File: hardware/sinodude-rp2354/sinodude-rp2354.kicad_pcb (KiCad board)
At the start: 2 copper layers, 68 x 36 mm, 93 parts, among them J1 USB-C, J2 SWD TC2030-IDC latching, J4 DUT, Q1 2N7002, SW1 BOOTSEL, SW2 RESET, U1 RP2354A, U2 AMS1117-3.3, U3 TPS2114APW, U4 SN74LVC8T245PW, U5 SN74LVC1T45DBV, U6 SN74LVC1T45DBV, Y1 12MHz/CL10pF/ESR50R/ABM8-272-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

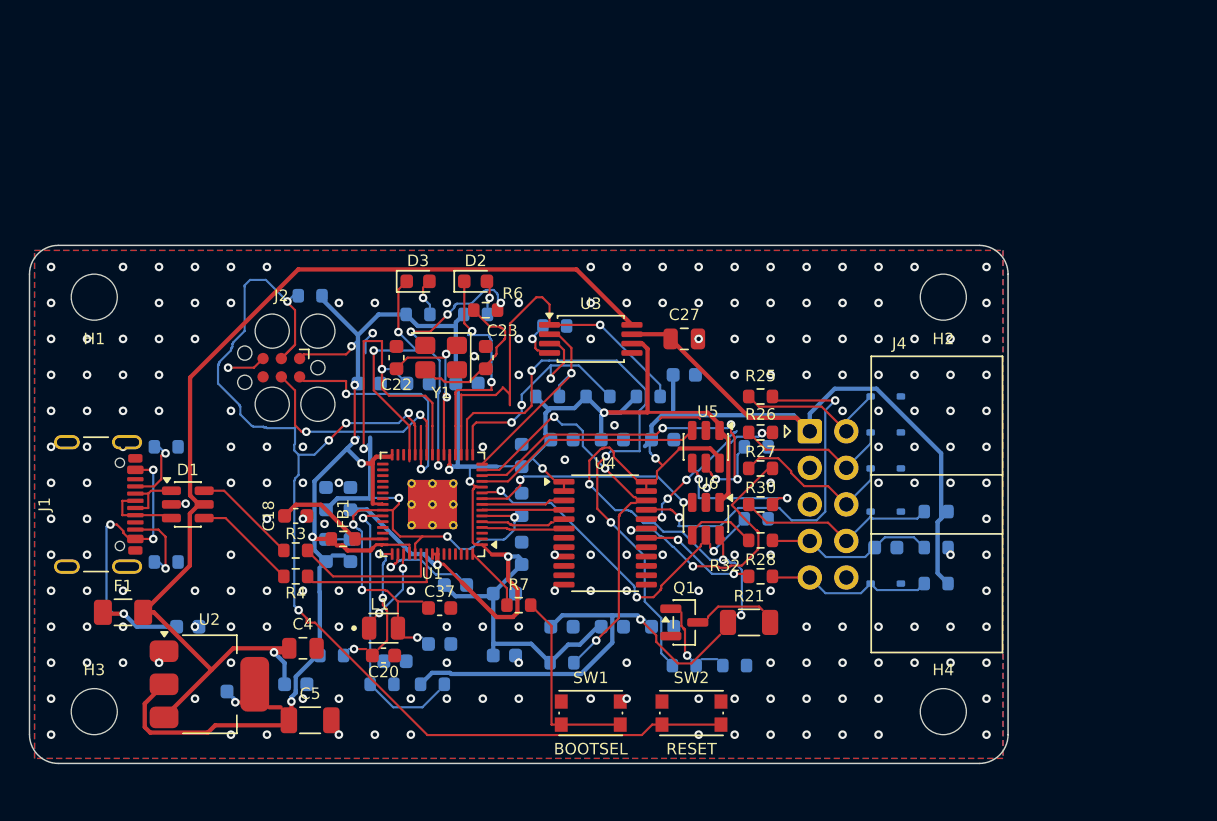
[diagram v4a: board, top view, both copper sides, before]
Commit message: hardware: cut both edges back so the connectors reach a case wall, 750 mA fuse
The board is 64 x 36 mm now, down from 68 x 36.

The west edge moves from x = 100 to 101.4, so J1's shell stands 1.4 mm proud
of the board instead of sitting flush with it. 1.4 mm is the geometric
maximum, not a choice: the receptacle's own shield tabs are plated slots
reaching x = 101.7 and the board has to hold them with 0.3 mm of copper
clearance. The east edge moves from 168 to 165.4, giving J4 2.1 mm of proud
shroud; that one could go further, since J4's pins stop at x = 157.6.

The four M3 holes now sit 3.2 mm in from both edges they meet, so each is on
its corner diagonal rather than 4.5 mm horizontally and 3.6 mm vertically.
3.2 mm is what U2's courtyard leaves for H3.

F1 becomes a Littelfuse 1206L075/16WR (C371166), 750 mA hold and 1.5 A trip,
in the same 1206 land. The 500 mA part it replaces held under 20% margin over
the 400 to 430 mA worst case before any ambient derating, sitting next to a
regulator burning 0.7 W. The new part is also lower resistance, 90 mohm
typical against 150. Its stock is thinner: about 6 k against 300 k.

Consequences absorbed: the outermost stitching via columns at x = 101.5 and
166.5 are gone with the copper they stood in, as is one via that the moved H2
crowded; J4's silk body outline is clipped at the edge it overhangs; J1's
reference designator moved back inside the board. Zone outlines follow the new
edges. DRC and ERC stay clean at every severity, GND is still one region, and
gerbers and drills still export.
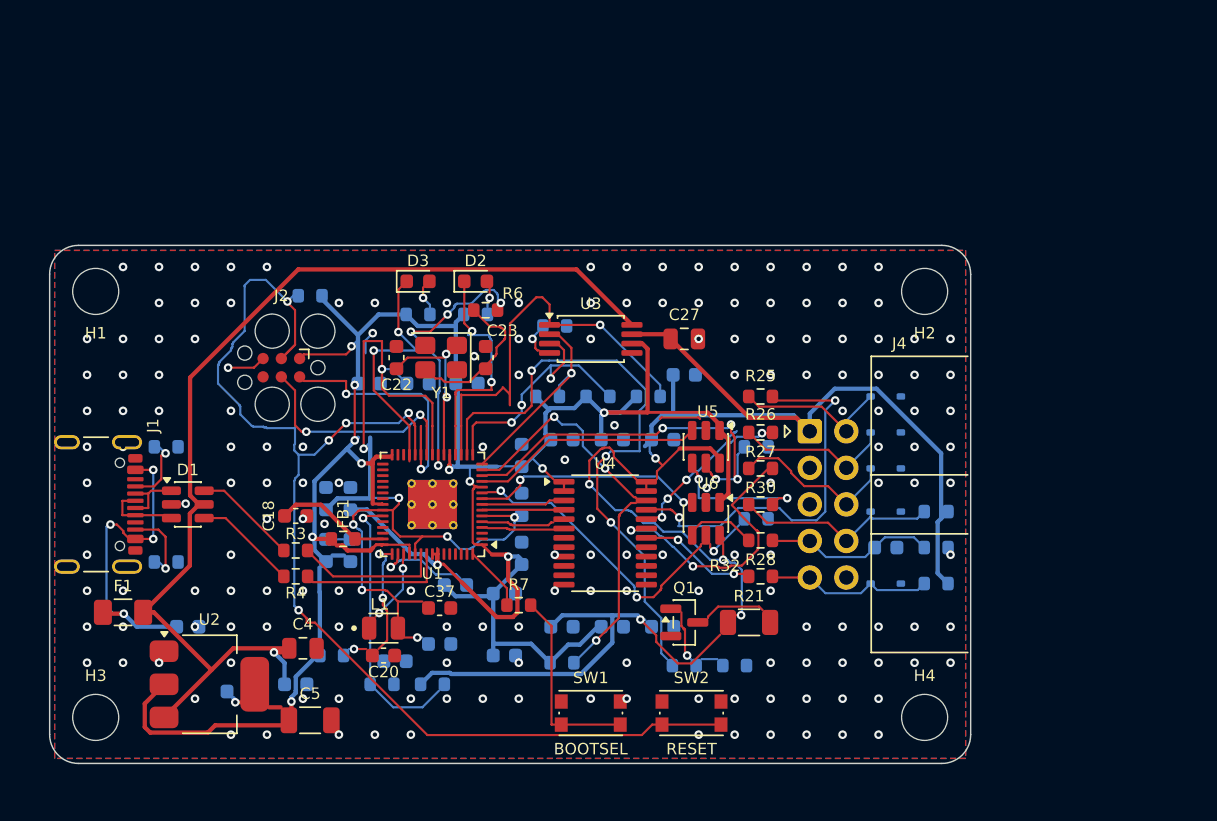
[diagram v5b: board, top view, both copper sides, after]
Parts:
- F1: value 500mA/Rmax300mR/F1206 -> 750mA/Rmax290mR/F1206
- moved H4 1.36 mm to (162.2, 134.8)
- moved H2 1.36 mm to (162.2, 105.2)
- moved H3 0.41 mm to (104.6, 134.8)
- moved H1 0.41 mm to (104.6, 105.2)
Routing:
- net GND: vias 198 -> 169
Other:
- board size 68 x 36 mm -> 64 x 36 mm

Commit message: hardware: centre the board on the page and fill in both title blocks
The outline sat at x 101.4-165.4, y 102-138 on an A4 sheet, which put it up
and to the left of centre. Everything (93 footprints, 1182 track items, 8
drawings, both zones) moved by +15.1, -15.0 mm, so the outline is now
116.5-180.5 by 87-123 and its centre lands on the A4 centre exactly.

The PCB had no title block at all. Both documents now carry the same one:
title, date, rev A, company, and the four comment lines the schematic already
had. The README's edge description loses its absolute coordinates, which this
move has just shown to be the wrong thing to write down; the distances that
actually matter stay.

DRC and ERC clean at every severity, GND still one region, tracks still on
0/45/90.
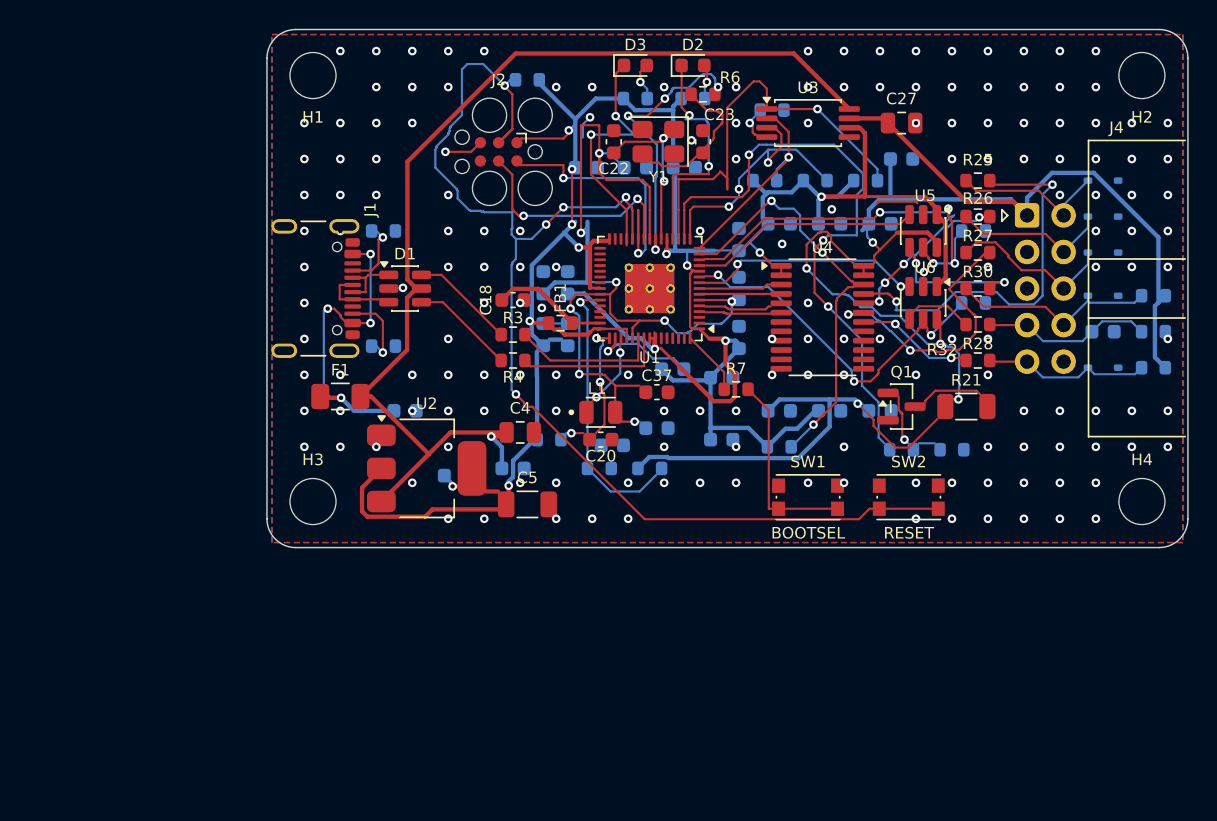
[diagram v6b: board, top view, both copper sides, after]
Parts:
- moved H4 21.3 mm to (177.3, 119.8)
- moved C13 21.3 mm to (149.3, 105.0)
- moved C23 21.3 mm to (146.8, 94.8)
- moved C7 21.3 mm to (149.3, 108.4)
- moved C8 21.3 mm to (149.3, 101.6)
- moved H2 21.3 mm to (177.3, 90.2)
- moved H3 21.3 mm to (119.7, 119.8)
- moved R6 21.3 mm to (146.8, 91.5)
- moved C11 21.3 mm to (137.4, 104.6)
- moved C12 21.3 mm to (137.4, 108.2)
- moved FB1 21.3 mm to (136.9, 107.4)
- moved H1 21.3 mm to (119.7, 90.2)
- moved J1 21.3 mm to (118.8, 105.0)
- moved C1 21.3 mm to (126.1, 113.5)
- moved C10 21.3 mm to (138.7, 96.6)
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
